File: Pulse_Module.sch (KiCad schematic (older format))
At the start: 1 part

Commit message: Питание и LM2596
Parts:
- CON3: renamed from CON?; footprint (none) -> Connect:BARREL_JACK
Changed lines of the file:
@@
 	2350 3750 3000 3750
 $Comp
-L GND #PWR02
+L GND #PWR01
 U 1 1 573A5270
 P 2550 4250
-F 0 "#PWR02" H 2550 4000 50  0001 C CNN
+F 0 "#PWR01" H 2550 4000 50  0001 C CNN
 F 1 "GND" H 2550 4100 50  0000 C CNN
 F 2 "" H 2550 4250 50  0000 C CNN
@@
 	2550 3850 2550 4250
 $Comp
-L BARREL_JACK CON?
+L BARREL_JACK CON3
 U 1 1 573A5D02
 P 2050 3850
-F 0 "CON?" H 2050 4100 50  0000 C CNN
+F 0 "CON3" H 2050 4100 50  0000 C CNN
 F 1 "BARREL_JACK" H 2050 3650 50  0000 C CNN
-F 2 "" H 2050 3850 50  0000 C CNN
+F 2 "Connect:BARREL_JACK" H 2050 3850 50  0001 C CNN
 F 3 "" H 2050 3850 50  0000 C CNN
 	1    2050 3850

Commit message: Готовая плата версия_1
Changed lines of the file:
@@
 LIBS:Pulse_Module-rescue
 LIBS:conn3
-LIBS:pl2303
 LIBS:power
 LIBS:device
@@
 F0 "Sheet56DEE0DD" 50
 F1 "ATmega1280.sch" 50
+F2 "Vcc" I L 4450 3750 60
 $EndSheet
-Text HLabel 4450 3750 2    60   Input ~ 0
-Vcc
 Wire Wire Line
 	3500 3750 4450 3750

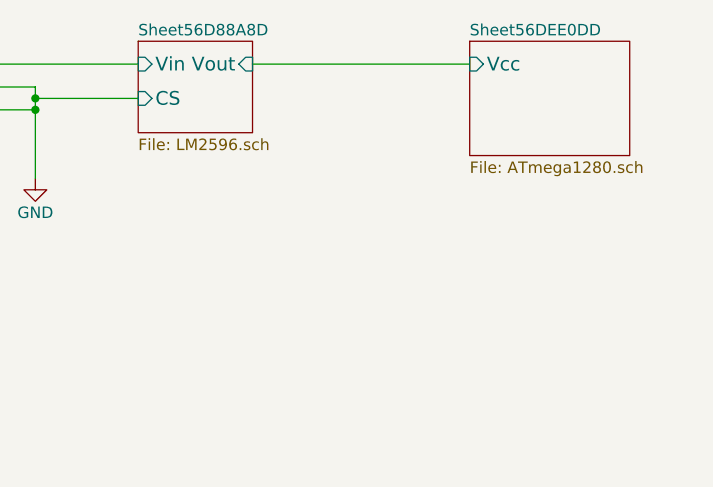
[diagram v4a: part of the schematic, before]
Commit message: Добавлен AMS1117 и изменения в питании
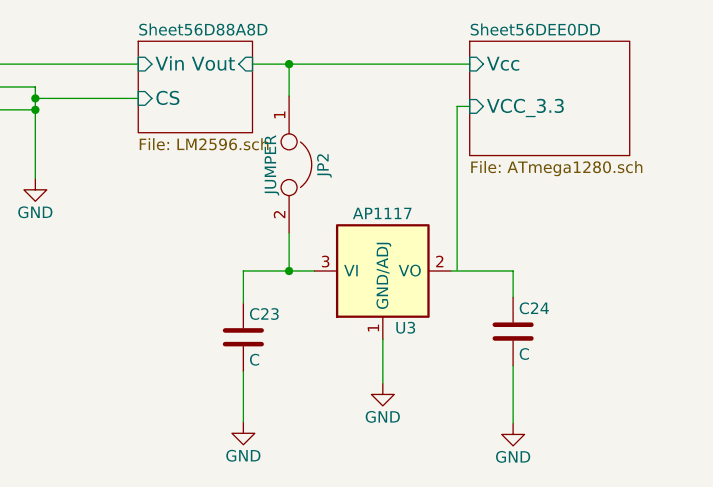
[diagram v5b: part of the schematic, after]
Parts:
- added C23, C24: C, Capacitors_SMD:C_0805, symbol C
- added JP2: JUMPER, Connect:PINHEAD1-2, symbol JUMPER
- added U3: AP1117, symbol AP1117
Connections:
- wire segments 6 -> 17
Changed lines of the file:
@@
 Comment4 ""
 $EndDescr
-$Sheet
-S 4450 3650 700  500
-U 56DEE0DE
-F0 "Sheet56DEE0DD" 50
-F1 "ATmega1280.sch" 50
-F2 "Vcc" I L 4450 3750 60
-$EndSheet
-$Sheet
-S 3000 3650 500  400
-U 56D88A8E
-F0 "Sheet56D88A8D" 50
-F1 "LM2596.sch" 50
-F2 "Vin" I L 3000 3750 60
-F3 "Vout" I R 3500 3750 60
-F4 "CS" I L 3000 3900 60
-$EndSheet
 $Comp
 L GND #PWR01
@@
 	1    0    0    -1
 $EndComp
+$Comp
+L AP1117 U3
+U 1 1 57F2F385
+P 4070 4655
+F 0 "U3" H 4170 4405 50  0000 C CNN
+F 1 "AP1117" H 4070 4905 50  0000 C CNN
+F 2 "" H 4070 4655 50  0001 C CNN
+F 3 "" H 4070 4655 50  0000 C CNN
+	1    4070 4655
+	1    0    0    -1
+$EndComp
+$Comp
+L C C23
+U 1 1 57F2F689
+P 3460 4945
+F 0 "C23" H 3485 5045 50  0000 L CNN
+F 1 "C" H 3485 4845 50  0000 L CNN
+F 2 "Capacitors_SMD:C_0805" H 3498 4795 50  0001 C CNN
+F 3 "" H 3460 4945 50  0000 C CNN
+	1    3460 4945
+	1    0    0    -1
+$EndComp
+$Comp
+L C C24
+U 1 1 57F2F6D4
+P 4640 4920
+F 0 "C24" H 4665 5020 50  0000 L CNN
+F 1 "C" H 4665 4820 50  0000 L CNN
+F 2 "Capacitors_SMD:C_0805" H 4678 4770 50  0001 C CNN
+F 3 "" H 4640 4920 50  0000 C CNN
+	1    4640 4920
+	1    0    0    -1
+$EndComp
+$Comp
+L GND #PWR02
+U 1 1 57F2F7B1
+P 3460 5315
+F 0 "#PWR02" H 3460 5065 50  0001 C CNN
+F 1 "GND" H 3460 5165 50  0000 C CNN
+F 2 "" H 3460 5315 50  0000 C CNN
+F 3 "" H 3460 5315 50  0000 C CNN
+	1    3460 5315
+	1    0    0    -1
+$EndComp
+$Comp
+L GND #PWR03
+U 1 1 57F2F900
+P 4640 5320
+F 0 "#PWR03" H 4640 5070 50  0001 C CNN
+F 1 "GND" H 4640 5170 50  0000 C CNN
+F 2 "" H 4640 5320 50  0000 C CNN
+F 3 "" H 4640 5320 50  0000 C CNN
+	1    4640 5320
+	1    0    0    -1
+$EndComp
+$Comp
+L GND #PWR04
+U 1 1 57F30351
+P 4070 5145
+F 0 "#PWR04" H 4070 4895 50  0001 C CNN
+F 1 "GND" H 4070 4995 50  0000 C CNN
+F 2 "" H 4070 5145 50  0000 C CNN
+F 3 "" H 4070 5145 50  0000 C CNN
+	1    4070 5145
+	1    0    0    -1
+$EndComp
+$Comp
+L JUMPER JP2
+U 1 1 57F32387
+P 3660 4190
+F 0 "JP2" H 3660 4340 50  0000 C CNN
+F 1 "JUMPER" H 3660 4110 50  0000 C CNN
+F 2 "Connect:PINHEAD1-2" H 3660 4190 50  0001 C CNN
+F 3 "" H 3660 4190 50  0000 C CNN
+	1    3660 4190
+	0    1    1    0
+$EndComp
+$Sheet
+S 3000 3650 500  400
+U 56D88A8E
+F0 "Sheet56D88A8D" 50
+F1 "LM2596.sch" 50
+F2 "Vin" I L 3000 3750 60
+F3 "Vout" I R 3500 3750 60
+F4 "CS" I L 3000 3900 60
+$EndSheet
 Wire Wire Line
 	2350 3750 3000 3750
@@
 Wire Wire Line
 	3500 3750 4450 3750
+Wire Wire Line
+	4640 5070 4640 5320
+Wire Wire Line
+	3460 5095 3460 5315
+Connection ~ 3660 4655
+Connection ~ 3660 3750
+Wire Wire Line
+	4070 4955 4070 5145
+Wire Wire Line
+	4370 4655 4640 4655
+Wire Wire Line
+	4640 4655 4640 4770
+Wire Wire Line
+	4395 4650 4395 3935
+Wire Wire Line
+	3660 3750 3660 3890
+Wire Wire Line
+	3460 4655 3460 4795
+$Sheet
+S 4450 3650 700  500
+U 56DEE0DE
+F0 "Sheet56DEE0DD" 50
+F1 "ATmega1280.sch" 50
+F2 "Vcc" I L 4450 3750 60
+F3 "VCC_3.3" I L 4450 3935 60
+$EndSheet
+Wire Wire Line
+	4395 3935 4450 3935
+Wire Wire Line
+	3460 4655 3770 4655
+Wire Wire Line
+	3660 4490 3660 4655
 $EndSCHEMATC

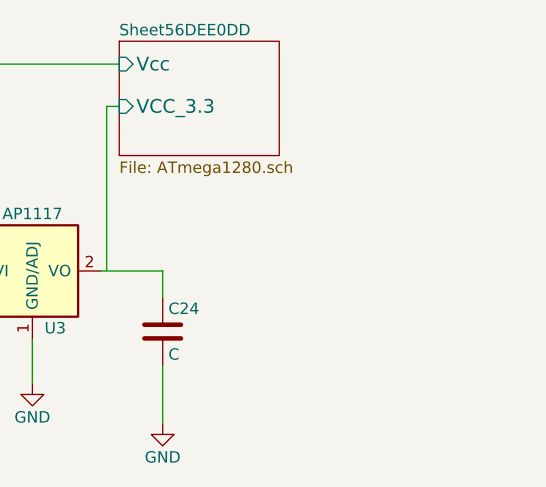
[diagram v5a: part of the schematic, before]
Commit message: Выбор футпринта для LMS1117
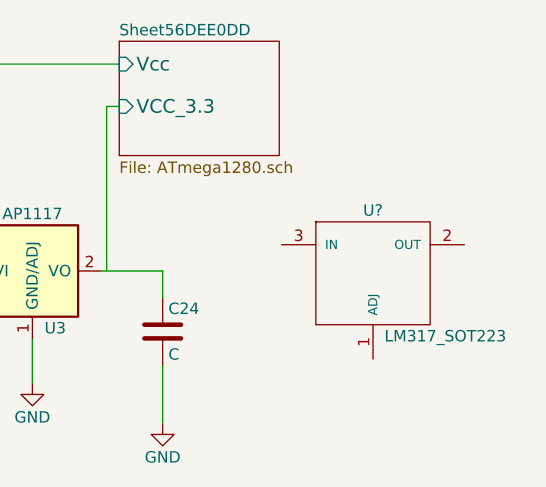
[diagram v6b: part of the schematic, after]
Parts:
- added U?: LM317_SOT223, symbol LM317_SOT223
- U3: footprint (none) -> TO_SOT_Packages_SMD:TO-252-2Lead
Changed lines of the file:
@@
 F 0 "U3" H 4170 4405 50  0000 C CNN
 F 1 "AP1117" H 4070 4905 50  0000 C CNN
-F 2 "" H 4070 4655 50  0001 C CNN
+F 2 "TO_SOT_Packages_SMD:TO-252-2Lead" H 4070 4655 50  0001 C CNN
 F 3 "" H 4070 4655 50  0000 C CNN
 	1    4070 4655
@@
 Wire Wire Line
 	3660 4490 3660 4655
+$Comp
+L LM317_SOT223 U?
+U 1 1 57F44B74
+P 5560 4690
+F 0 "U?" H 5560 4990 50  0000 C CNN
+F 1 "LM317_SOT223" H 5610 4440 50  0000 L CNN
+F 2 "" H 5560 4690 50  0000 C CNN
+F 3 "" H 5560 4690 50  0000 C CNN
+	1    5560 4690
+	1    0    0    -1
+$EndComp
 $EndSCHEMATC

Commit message: Изменения футпринтов
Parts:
- removed U3: AP1117, TO_SOT_Packages_SMD:TO-252-2Lead, symbol AP1117
- removed U?: LM317_SOT223, symbol LM317_SOT223
- added U3: AMS1117, TO_SOT_Packages_SMD:TO-252-2Lead, symbol AMS1117
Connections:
- wire segments 17 -> 21
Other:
- moved on the sheet: C23, C24
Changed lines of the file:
@@
 LIBS:contrib
 LIBS:valves
+LIBS:AMS1117
 LIBS:Pulse_Module-cache
 EELAYER 25 0
@@
 $EndComp
 $Comp
-L AP1117 U3
-U 1 1 57F2F385
-P 4070 4655
-F 0 "U3" H 4170 4405 50  0000 C CNN
-F 1 "AP1117" H 4070 4905 50  0000 C CNN
-F 2 "TO_SOT_Packages_SMD:TO-252-2Lead" H 4070 4655 50  0001 C CNN
-F 3 "" H 4070 4655 50  0000 C CNN
-	1    4070 4655
-	1    0    0    -1
-$EndComp
-$Comp
-L C C23
-U 1 1 57F2F689
-P 3460 4945
-F 0 "C23" H 3485 5045 50  0000 L CNN
-F 1 "C" H 3485 4845 50  0000 L CNN
-F 2 "Capacitors_SMD:C_0805" H 3498 4795 50  0001 C CNN
-F 3 "" H 3460 4945 50  0000 C CNN
-	1    3460 4945
-	1    0    0    -1
-$EndComp
-$Comp
 L C C24
 U 1 1 57F2F6D4
-P 4640 4920
-F 0 "C24" H 4665 5020 50  0000 L CNN
-F 1 "C" H 4665 4820 50  0000 L CNN
-F 2 "Capacitors_SMD:C_0805" H 4678 4770 50  0001 C CNN
-F 3 "" H 4640 4920 50  0000 C CNN
-	1    4640 4920
+P 5210 5215
+F 0 "C24" H 5235 5315 50  0000 L CNN
+F 1 "C" H 5235 5115 50  0000 L CNN
+F 2 "Capacitors_SMD:C_0805" H 5248 5065 50  0001 C CNN
+F 3 "" H 5210 5215 50  0000 C CNN
+	1    5210 5215
 	1    0    0    -1
 $EndComp
@@
 L GND #PWR02
 U 1 1 57F2F7B1
-P 3460 5315
-F 0 "#PWR02" H 3460 5065 50  0001 C CNN
-F 1 "GND" H 3460 5165 50  0000 C CNN
-F 2 "" H 3460 5315 50  0000 C CNN
-F 3 "" H 3460 5315 50  0000 C CNN
-	1    3460 5315
+P 4180 5550
+F 0 "#PWR02" H 4180 5300 50  0001 C CNN
+F 1 "GND" H 4180 5400 50  0000 C CNN
+F 2 "" H 4180 5550 50  0000 C CNN
+F 3 "" H 4180 5550 50  0000 C CNN
+	1    4180 5550
 	1    0    0    -1
 $EndComp
@@
 L GND #PWR03
 U 1 1 57F2F900
-P 4640 5320
-F 0 "#PWR03" H 4640 5070 50  0001 C CNN
-F 1 "GND" H 4640 5170 50  0000 C CNN
-F 2 "" H 4640 5320 50  0000 C CNN
-F 3 "" H 4640 5320 50  0000 C CNN
-	1    4640 5320
+P 5210 5475
+F 0 "#PWR03" H 5210 5225 50  0001 C CNN
+F 1 "GND" H 5210 5325 50  0000 C CNN
+F 2 "" H 5210 5475 50  0000 C CNN
+F 3 "" H 5210 5475 50  0000 C CNN
+	1    5210 5475
 	1    0    0    -1
 $EndComp
@@
 L GND #PWR04
 U 1 1 57F30351
-P 4070 5145
-F 0 "#PWR04" H 4070 4895 50  0001 C CNN
-F 1 "GND" H 4070 4995 50  0000 C CNN
-F 2 "" H 4070 5145 50  0000 C CNN
-F 3 "" H 4070 5145 50  0000 C CNN
-	1    4070 5145
+P 4155 6805
+F 0 "#PWR04" H 4155 6555 50  0001 C CNN
+F 1 "GND" H 4155 6655 50  0000 C CNN
+F 2 "" H 4155 6805 50  0000 C CNN
+F 3 "" H 4155 6805 50  0000 C CNN
+	1    4155 6805
 	1    0    0    -1
 $EndComp
@@
 Wire Wire Line
 	3500 3750 4450 3750
-Wire Wire Line
-	4640 5070 4640 5320
-Wire Wire Line
-	3460 5095 3460 5315
-Connection ~ 3660 4655
 Connection ~ 3660 3750
 Wire Wire Line
-	4070 4955 4070 5145
-Wire Wire Line
-	4370 4655 4640 4655
-Wire Wire Line
-	4640 4655 4640 4770
-Wire Wire Line
-	4395 4650 4395 3935
-Wire Wire Line
 	3660 3750 3660 3890
-Wire Wire Line
-	3460 4655 3460 4795
 $Sheet
 S 4450 3650 700  500
@@
 Wire Wire Line
 	4395 3935 4450 3935
-Wire Wire Line
-	3460 4655 3770 4655
-Wire Wire Line
-	3660 4490 3660 4655
 $Comp
-L LM317_SOT223 U?
-U 1 1 57F44B74
-P 5560 4690
-F 0 "U?" H 5560 4990 50  0000 C CNN
-F 1 "LM317_SOT223" H 5610 4440 50  0000 L CNN
-F 2 "" H 5560 4690 50  0000 C CNN
-F 3 "" H 5560 4690 50  0000 C CNN
-	1    5560 4690
+L AMS1117 U3
+U 1 1 57F689F7
+P 4180 4945
+F 0 "U3" H 4180 4845 50  0000 C CNN
+F 1 "AMS1117" H 4180 5045 50  0000 C CNN
+F 2 "TO_SOT_Packages_SMD:TO-252-2Lead" H 4180 4945 60  0001 C CNN
+F 3 "" H 4180 4945 60  0000 C CNN
+	1    4180 4945
 	1    0    0    -1
 $EndComp
+$Comp
+L C C23
+U 1 1 57F2F689
+P 3085 5220
+F 0 "C23" H 3110 5320 50  0000 L CNN
+F 1 "C" H 3110 5120 50  0000 L CNN
+F 2 "Capacitors_SMD:C_0805" H 3123 5070 50  0001 C CNN
+F 3 "" H 3085 5220 50  0000 C CNN
+	1    3085 5220
+	1    0    0    -1
+$EndComp
+Wire Wire Line
+	3660 4490 3660 4635
+Wire Wire Line
+	3660 4635 3235 4635
+Wire Wire Line
+	3235 4635 3235 4945
+Wire Wire Line
+	3085 4945 3380 4945
+Wire Wire Line
+	3085 4945 3085 5070
+Connection ~ 3235 4945
+$Comp
+L GND #PWR05
+U 1 1 57F69DF6
+P 3085 5530
+F 0 "#PWR05" H 3085 5280 50  0001 C CNN
+F 1 "GND" H 3085 5380 50  0000 C CNN
+F 2 "" H 3085 5530 50  0000 C CNN
+F 3 "" H 3085 5530 50  0000 C CNN
+	1    3085 5530
+	1    0    0    -1
+$EndComp
+Wire Wire Line
+	3085 5370 3085 5530
+Wire Wire Line
+	4180 5445 4180 5550
+Wire Wire Line
+	4980 4945 5210 4945
+Wire Wire Line
+	5210 4945 5210 5065
+Wire Wire Line
+	5210 5365 5210 5475
+Wire Wire Line
+	4395 3935 4395 4650
+Wire Wire Line
+	4395 4650 5045 4650
+Wire Wire Line
+	5045 4650 5045 4945
+Connection ~ 5045 4945
 $EndSCHEMATC

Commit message: небольшие изменения
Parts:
- C23: value C -> 10uF
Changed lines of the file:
@@
 L GND #PWR02
 U 1 1 57F2F7B1
-P 4180 5550
-F 0 "#PWR02" H 4180 5300 50  0001 C CNN
-F 1 "GND" H 4180 5400 50  0000 C CNN
-F 2 "" H 4180 5550 50  0000 C CNN
-F 3 "" H 4180 5550 50  0000 C CNN
-	1    4180 5550
-	1    0    0    -1
-$EndComp
-$Comp
-L GND #PWR03
-U 1 1 57F2F900
-P 5210 5475
-F 0 "#PWR03" H 5210 5225 50  0001 C CNN
-F 1 "GND" H 5210 5325 50  0000 C CNN
-F 2 "" H 5210 5475 50  0000 C CNN
-F 3 "" H 5210 5475 50  0000 C CNN
-	1    5210 5475
+P 4180 5785
+F 0 "#PWR02" H 4180 5535 50  0001 C CNN
+F 1 "GND" H 4180 5635 50  0000 C CNN
+F 2 "" H 4180 5785 50  0000 C CNN
+F 3 "" H 4180 5785 50  0000 C CNN
+	1    4180 5785
 	1    0    0    -1
 $EndComp
@@
 F4 "CS" I L 3000 3900 60
 $EndSheet
+$Sheet
+S 4450 3650 700  500
+U 56DEE0DE
+F0 "Sheet56DEE0DD" 50
+F1 "ATmega1280.sch" 50
+F2 "Vcc" I L 4450 3750 60
+F3 "VCC_3.3" I L 4450 3935 60
+$EndSheet
+$Comp
+L AMS1117 U3
+U 1 1 57F689F7
+P 4180 4945
+F 0 "U3" H 4180 4845 50  0000 C CNN
+F 1 "AMS1117" H 4180 5045 50  0000 C CNN
+F 2 "TO_SOT_Packages_SMD:TO-252-2Lead" H 4180 4945 60  0001 C CNN
+F 3 "" H 4180 4945 60  0000 C CNN
+	1    4180 4945
+	1    0    0    -1
+$EndComp
+$Comp
+L C C23
+U 1 1 57F2F689
+P 3085 5220
+F 0 "C23" H 3110 5320 50  0000 L CNN
+F 1 "10uF" H 3110 5120 50  0000 L CNN
+F 2 "Capacitors_SMD:C_0805" H 3123 5070 50  0001 C CNN
+F 3 "" H 3085 5220 50  0000 C CNN
+	1    3085 5220
+	1    0    0    -1
+$EndComp
 Wire Wire Line
 	2350 3750 3000 3750
@@
 Wire Wire Line
 	3660 3750 3660 3890
-$Sheet
-S 4450 3650 700  500
-U 56DEE0DE
-F0 "Sheet56DEE0DD" 50
-F1 "ATmega1280.sch" 50
-F2 "Vcc" I L 4450 3750 60
-F3 "VCC_3.3" I L 4450 3935 60
-$EndSheet
 Wire Wire Line
 	4395 3935 4450 3935
-$Comp
-L AMS1117 U3
-U 1 1 57F689F7
-P 4180 4945
-F 0 "U3" H 4180 4845 50  0000 C CNN
-F 1 "AMS1117" H 4180 5045 50  0000 C CNN
-F 2 "TO_SOT_Packages_SMD:TO-252-2Lead" H 4180 4945 60  0001 C CNN
-F 3 "" H 4180 4945 60  0000 C CNN
-	1    4180 4945
-	1    0    0    -1
-$EndComp
-$Comp
-L C C23
-U 1 1 57F2F689
-P 3085 5220
-F 0 "C23" H 3110 5320 50  0000 L CNN
-F 1 "C" H 3110 5120 50  0000 L CNN
-F 2 "Capacitors_SMD:C_0805" H 3123 5070 50  0001 C CNN
-F 3 "" H 3085 5220 50  0000 C CNN
-	1    3085 5220
-	1    0    0    -1
-$EndComp
 Wire Wire Line
 	3660 4490 3660 4635
@@
 	3085 4945 3085 5070
 Connection ~ 3235 4945
-$Comp
-L GND #PWR05
-U 1 1 57F69DF6
-P 3085 5530
-F 0 "#PWR05" H 3085 5280 50  0001 C CNN
-F 1 "GND" H 3085 5380 50  0000 C CNN
-F 2 "" H 3085 5530 50  0000 C CNN
-F 3 "" H 3085 5530 50  0000 C CNN
-	1    3085 5530
-	1    0    0    -1
-$EndComp
-Wire Wire Line
-	3085 5370 3085 5530
-Wire Wire Line
-	4180 5445 4180 5550
 Wire Wire Line
 	4980 4945 5210 4945
 Wire Wire Line
 	5210 4945 5210 5065
-Wire Wire Line
-	5210 5365 5210 5475
 Wire Wire Line
 	4395 3935 4395 4650
@@
 	5045 4650 5045 4945
 Connection ~ 5045 4945
+Wire Wire Line
+	3085 5370 3085 5615
+Wire Wire Line
+	3085 5615 5210 5615
+Wire Wire Line
+	5210 5615 5210 5365
+Wire Wire Line
+	4180 5445 4180 5785
+Connection ~ 4180 5615
 $EndSCHEMATC
